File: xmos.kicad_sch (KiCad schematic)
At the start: 93 parts, among them J3 XMOS JTAG, J4 XTAG DEV, Q1 LBSS138WT1G, Q2 LBSS138WT1G, Q3 BC847B, U10 SN74LVC125APWR, U11 TLV73333PDBVR, U8 XU316-1024-QF60B-C24​, U9 W25Q32JVSSIQ, X1 24MHz 12pF

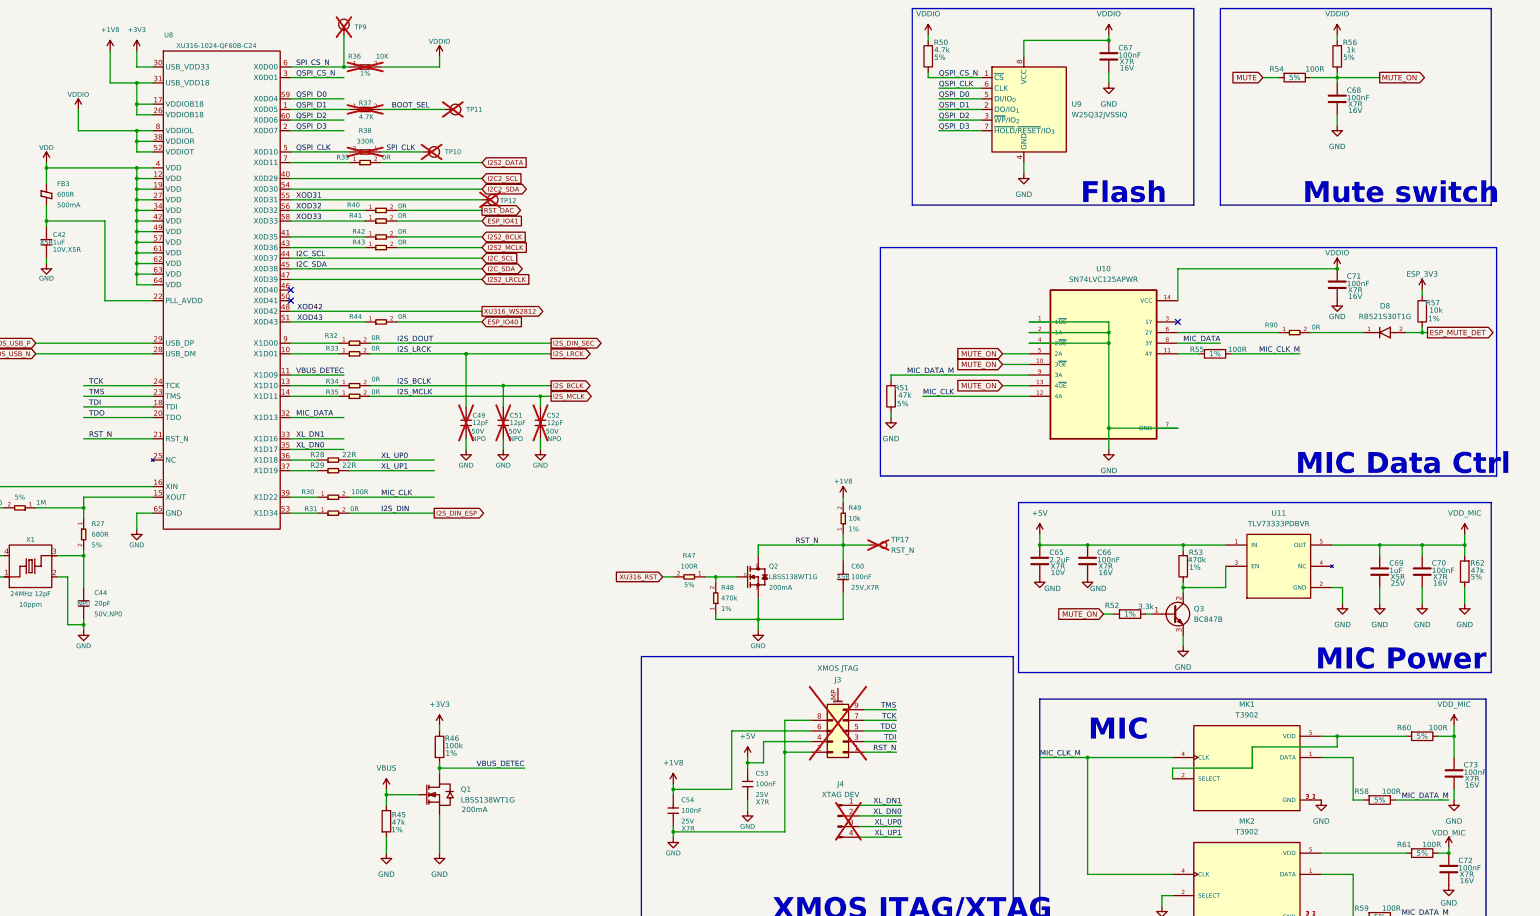
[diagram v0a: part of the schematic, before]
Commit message: v2 hardware revision
MPR121 touch controller added to replace esp32-s3 integrated touch pins
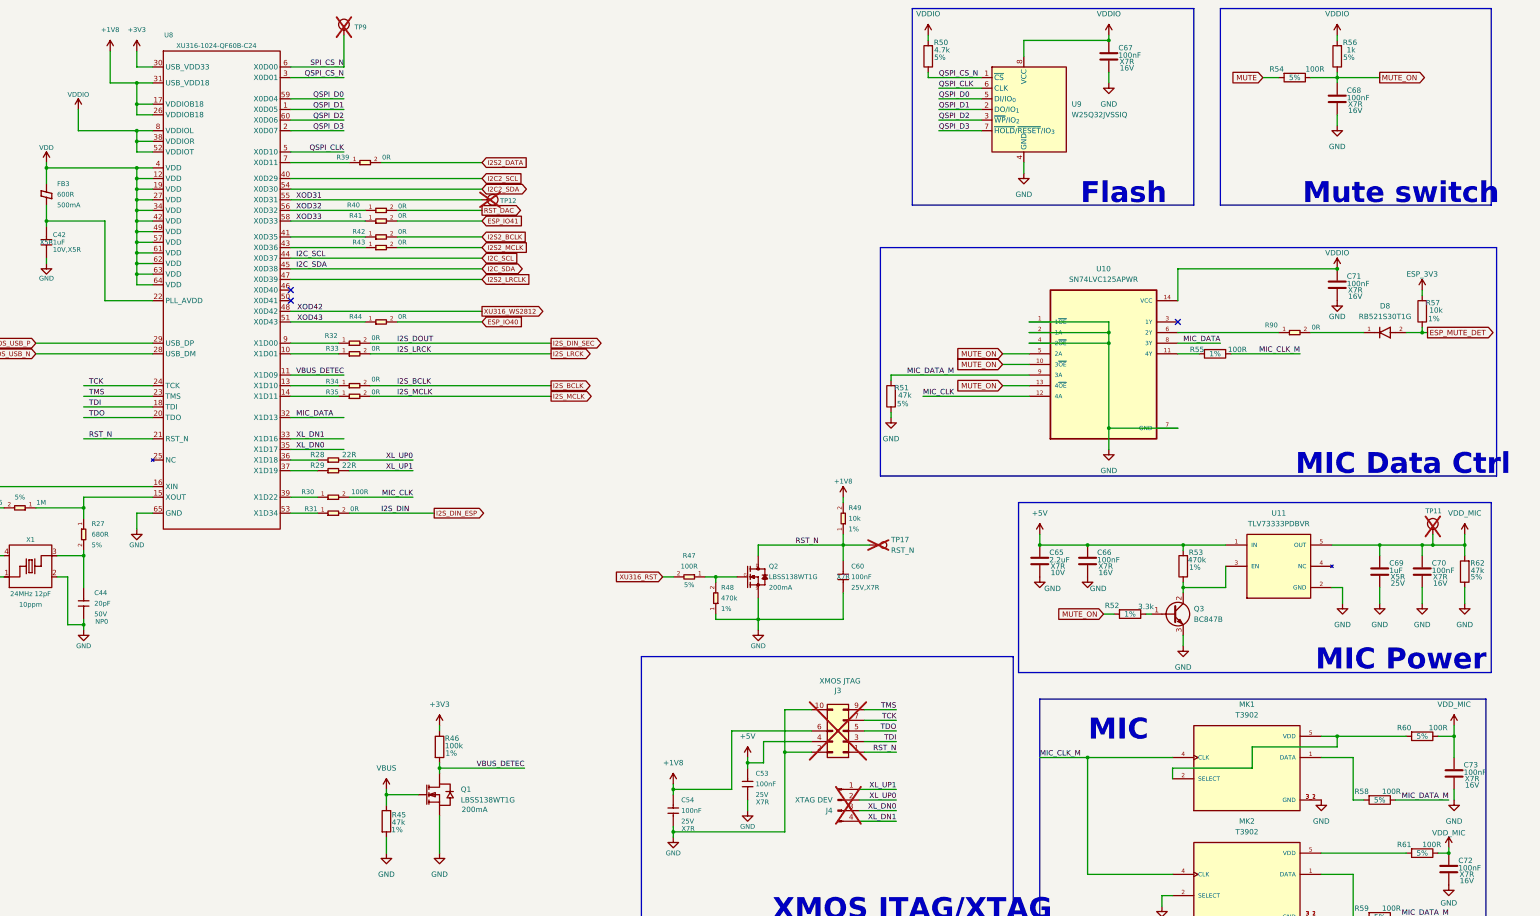
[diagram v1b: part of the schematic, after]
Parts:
- removed C49, C51, C52: 12pF, Capacitor_SMD:C_0402_1005Metric, symbol Seeed_libdb:Capacitors/302010049
- removed R36: 10K, Resistor_SMD:R_0402_1005Metric, symbol Seeed_libdb:Resistors/301010047
- removed R37: 4.7K, Resistor_SMD:R_0402_1005Metric, symbol Seeed_libdb:Resistors/301010010
- removed R38: 330R, Resistor_SMD:R_0402_1005Metric, symbol Seeed_libadl:Resistors/301010466
- removed TP10: TEST-POINT, TestPoint:TestPoint_Pad_D1.0mm, symbol 0_Seeed_Misc:TEST-POINT
- C40: Function (none) -> XMOS; SKU 302010050 -> (none); Status Tracker -> (none)
- C42: Function (none) -> XMOS; SKU 302013249 -> (none); Status HA Voice KIT -> (none)
- C44: Function (none) -> XMOS; SKU 302010050 -> (none); Status Tracker -> (none); Temperature -55°C to 125°C -> (none); Voltage Rating 50V,NP0 -> 50V
- C53, C54: Function (none) -> POWER; SKU 302010024 -> (none)
- C60: Dielectric X5R -> X7R; Function (none) -> POWER; SKU 302010024 -> (none); Status BeagleBone Carrier Board -> (none); Supplier Part C1525 -> (none)
- D8: Availability In Stock -> (none); Check_prices https://www.snapeda.com/parts/RB521S30T1G/Onsemi/view-part/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 -> (none); PARTREV 7/11/1905 -> (none)
- FB3: Function (none) -> XMOS; SKU 303030521 -> (none); Status ReCamera-Pre -> (none)
- FB4: Part number BLM18AG121SN1D -> (none)
- FB5: Part number BLM18AG601SN1D -> (none)
- MK1, MK2: Availability Not in stock -> (none); Check_prices https://www.snapeda.com/parts/T3902/TDK/view-part/?ref=eda -> (none); PARTREV 1.0 -> (none)
- Q1: Supplier LCSC -> (none); Supplier Part C383201 -> (none)
- Q2: Function (none) -> XMOS; SKU 305031542 -> (none); Supplier Part C383201 -> (none)
- R26: Function (none) -> XMOS; SKU 301010009 -> (none); Status reSpeaker -> (none)
- R27: Function (none) -> XMOS; SKU 301010505 -> (none); Status Combox Pro -> (none)
- R28, R29: Function (none) -> XMOS; SKU 301010002 -> (none); Status BeagleBone Carrier Board -> (none)
- R30: Function (none) -> XMOS; SKU 301010028 -> (none); Status BeagleBone Carrier Board -> (none)
- R31, R32, R33, R34, R35, R41, R42, R43, R44, R90: Function (none) -> XMOS; SKU 301010000 -> (none); Status BeagleBone Carrier Board -> (none)
- R39, R40: Function (none) -> XMOS; SKU 301010000 -> (none)
- R47: SKU 301010028 -> (none); Status BeagleBone Carrier Board -> (none); Supplier Part C25076 -> (none)
- R48: SKU 301010069 -> (none); Status Combox Pro -> (none); Supplier Part C25790 -> (none)
- R49: SKU 301010047 -> (none); Status BeagleBone Carrier Board -> (none); Supplier Part C25744 -> (none)
- R54: Power Rating (none) -> 5%
- TP12: SKU TP45C_SMD -> (none)
- U10: Availability In Stock -> (none); Check_prices https://www.snapeda.com/parts/SN74LVC125APWR/Texas+Instrume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 -> (none)
- U11: Availability In Stock -> (none); Check_prices https://www.snapeda.com/parts/TLV73333PDBVR/Texas+Instrumen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 -> (none); PARTREV C -> (none)
- U8: Function (none) -> XMOS; SKU 310011736 -> (none)
- X1: Function (none) -> XMOS; SKU 306011444 -> (none); Status AI VISION 2 -> (none)
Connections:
- net BOOT_SEL is gone; now on net VDD_MIC: TP11.1 (T)
- net GND: now also J3.10 (Pin_10); no longer J3.8 (Pin_8)
- net XL_DN0: now also J4.3 (Pin_3); no longer J4.2 (Pin_2)
- net XL_DN1: now also J4.4 (Pin_4); no longer J4.1 (Pin_1)
- net XL_UP0: now also J4.2 (Pin_2); no longer J4.3 (Pin_3)
- net XL_UP1: now also J4.1 (Pin_1); no longer J4.4 (Pin_4)
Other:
- moved on the sheet: J4
